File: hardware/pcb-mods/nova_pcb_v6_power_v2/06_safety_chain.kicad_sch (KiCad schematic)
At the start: 23 parts, among them Q2 BSS138_cutoff, Q3 BSS138_estop, Q4 BSS138_jetcut, SW2 Estop_NC_latching, U10 INA226, U11 INA226, U8 LM393, U9 INA226

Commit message: pcb(v6-power-v2): backfill MPN + Manufacturer fields — 100% BOM coverage
All 50 BOM components now carry MPNs from the verified order list:
Yageo RC0603 resistor set (R14 470k = Vishay CRCW0603 DigiKey sub),
Nichicon UPW1E bulk caps, Bourns SRR1260-220M, Infineon IRLB3034PBF,
onsemi BSS138 x3, TI LM393DR, Pololu buck modules (off-board),
GODIY INA226 20A R002 modules with I2C addresses in Manufacturer field,
AMASS XT60H/XT30U, JST B3B-XH-A, Adam Tech BHR-12-VUA, Sullins headers.
ERC: 0 errors (1 expected V7V5_ARM warning). kicad-happy bom_lock: pass.

Co-Authored-By: Claude Fable 5 <noreply@anthropic.com>
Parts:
- C7: MPN (none) -> CC0603KRX7R9BB104; Manufacturer (none) -> Yageo
- Q2, Q3, Q4: MPN (none) -> BSS138; Manufacturer (none) -> onsemi
- R11, R12: MPN (none) -> RC0603FR-074K7L; Manufacturer (none) -> Yageo
- R13, R5, R7, R8, R9: MPN (none) -> RC0603FR-0710KL; Manufacturer (none) -> Yageo
- R14: MPN (none) -> CRCW0603470KFKEA; Manufacturer (none) -> Vishay Dale
- R15: MPN (none) -> RC0603FR-071ML; Manufacturer (none) -> Yageo
- R16, R2: MPN (none) -> RC0603FR-07100KL; Manufacturer (none) -> Yageo
- R3: MPN (none) -> RC0603FR-0722KL; Manufacturer (none) -> Yageo
- R4: MPN (none) -> RC0603FR-0711K3L; Manufacturer (none) -> Yageo
- R6: MPN (none) -> RC0603FR-0712K1L; Manufacturer (none) -> Yageo
- SW2: MPN (none) -> KF301-5.0-2P; Manufacturer (none) -> Generic (Tugermoola kit; wires to Mxuteuk HB2-ES544)
- U10: MPN (none) -> INA226-20A-R002-MODULE; Manufacturer (none) -> GODIYMODULES (Amazon, off-board, addr 0x41)
- U11: MPN (none) -> INA226-20A-R002-MODULE; Manufacturer (none) -> GODIYMODULES (Amazon, off-board, addr 0x44)
- U8: MPN (none) -> LM393DR; Manufacturer (none) -> Texas Instruments
- U9: MPN (none) -> INA226-20A-R002-MODULE; Manufacturer (none) -> GODIYMODULES (Amazon, off-board, addr 0x40)

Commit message: pcb(v6-power-v2): correct C1-C5 to FymuSing (as purchased) + DigiKey PNs from order CSV
Verified against Complete_Digikey_Order_NOVA.csv (16 lines, all match):
R14 470k confirmed Vishay CRCW0603470KFKEA (541-470KHCT-ND).
C1-C5 corrected Nichicon->FymuSing 1000uF/25V (Amazon purchase, 10x17mm).
Remaining 23 parts without DigiKey PN are Amazon/Pololu/AMASS sourced.

Co-Authored-By: Claude Fable 5 <noreply@anthropic.com>
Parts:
- C7: DigiKey (none) -> 311-1344-1-ND
- Q2, Q3, Q4: DigiKey (none) -> BSS138CT-ND
- R11, R12: DigiKey (none) -> 311-4.70KHRCT-ND
- R13, R5, R7, R8, R9: DigiKey (none) -> 311-10.0KHRCT-ND
- R14: DigiKey (none) -> 541-470KHCT-ND
- R15: DigiKey (none) -> 311-1.00MHRCT-ND
- R16, R2: DigiKey (none) -> 311-100KHRCT-ND
- R3: DigiKey (none) -> 311-22.0KHRCT-ND
- R4: DigiKey (none) -> 311-11.3KHRCT-ND
- R6: DigiKey (none) -> 311-12.1KHRCT-ND
- U8: DigiKey (none) -> 296-1015-1-ND
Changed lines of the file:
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@@
 			)
 		)
+		(property "DigiKey" "311-10.0KHRCT-ND" (at 0 0 0)
+			(effects
+				(font
+					(size 1.27 1.27)
+				)
+				(hide yes)
+			)
+		)
 		(pin "1"
 		)
@@
 			)
 		)
+		(property "DigiKey" "311-4.70KHRCT-ND" (at 0 0 0)
+			(effects
+				(font
+					(size 1.27 1.27)
+				)
+				(hide yes)
+			)
+		)
 		(pin "1"
 		)
@@
 			)
 		)
+		(property "DigiKey" "BSS138CT-ND" (at 0 0 0)
+			(effects
+				(font
+					(size 1.27 1.27)
+				)
+				(hide yes)
+			)
+		)
 		(pin "1"
 		)
@@
 			)
 		)
+		(property "DigiKey" "311-10.0KHRCT-ND" (at 0 0 0)
+			(effects
+				(font
+					(size 1.27 1.27)
+				)
+				(hide yes)
+			)
+		)
 		(pin "1"
 		)
@@
 			)
 		)
+		(property "DigiKey" "311-10.0KHRCT-ND" (at 0 0 0)
+			(effects
+				(font
+					(size 1.27 1.27)
+				)
+				(hide yes)
+			)
+		)
 		(pin "1"
 		)
@@
 			)
 		)
+		(property "DigiKey" "296-1015-1-ND" (at 0 0 0)
+			(effects
+				(font
+					(size 1.27 1.27)
+				)
+				(hide yes)
+			)
+		)
 		(pin "8"
 		)
@@
 			)
 		)
+		(property "DigiKey" "311-22.0KHRCT-ND" (at 0 0 0)
+			(effects
+				(font
+					(size 1.27 1.27)
+				)
+				(hide yes)
+			)
+		)
 		(pin "1"
 		)
@@
 			)
 		)
+		(property "DigiKey" "296-1015-1-ND" (at 0 0 0)
+			(effects
+				(font
+					(size 1.27 1.27)
+				)
+				(hide yes)
+			)
+		)
 		(pin "3"
 		)
@@
 			)
 		)
+		(property "DigiKey" "311-4.70KHRCT-ND" (at 0 0 0)
+			(effects
+				(font
+					(size 1.27 1.27)
+				)
+				(hide yes)
+			)
+		)
 		(pin "1"
 		)
@@
 			)
 		)
+		(property "DigiKey" "311-12.1KHRCT-ND" (at 0 0 0)
+			(effects
+				(font
+					(size 1.27 1.27)
+				)
+				(hide yes)
+			)
+		)
 		(pin "1"
 		)
@@
 			)
 		)
+		(property "DigiKey" "311-11.3KHRCT-ND" (at 0 0 0)
+			(effects
+				(font
+					(size 1.27 1.27)
+				)
+				(hide yes)
+			)
+		)
 		(pin "1"
 		)
@@
 			)
 		)
+		(property "DigiKey" "311-10.0KHRCT-ND" (at 0 0 0)
+			(effects
+				(font
+					(size 1.27 1.27)
+				)
+				(hide yes)
+			)
+		)
 		(pin "1"
 		)
@@
 			)
 		)
+		(property "DigiKey" "296-1015-1-ND" (at 0 0 0)
+			(effects
+				(font
+					(size 1.27 1.27)
+				)
+				(hide yes)
+			)
+		)
 		(pin "5"
 		)
@@
 			)
 		)
+		(property "DigiKey" "311-100KHRCT-ND" (at 0 0 0)
+			(effects
+				(font
+					(size 1.27 1.27)
+				)
+				(hide yes)
+			)
+		)
 		(pin "1"
 		)
@@
 			)
 		)
+		(property "DigiKey" "311-10.0KHRCT-ND" (at 0 0 0)
+			(effects
+				(font
+					(size 1.27 1.27)
+				)
+				(hide yes)
+			)
+		)
 		(pin "1"
 		)
@@
 			)
 		)
+		(property "DigiKey" "541-470KHCT-ND" (at 0 0 0)
+			(effects
+				(font
+					(size 1.27 1.27)
+				)
+				(hide yes)
+			)
+		)
 		(pin "1"
 		)
@@
 			)
 		)
+		(property "DigiKey" "311-1.00MHRCT-ND" (at 0 0 0)
+			(effects
+				(font
+					(size 1.27 1.27)
+				)
+				(hide yes)
+			)
+		)
 		(pin "1"
 		)
@@
 			)
 		)
+		(property "DigiKey" "311-1344-1-ND" (at 0 0 0)
+			(effects
+				(font
+					(size 1.27 1.27)
+				)
+				(hide yes)
+			)
+		)
 		(pin "1"
 		)
@@
 			)
 		)
+		(property "DigiKey" "BSS138CT-ND" (at 0 0 0)
+			(effects
+				(font
+					(size 1.27 1.27)
+				)
+				(hide yes)
+			)
+		)
 		(pin "1"
 		)
@@
 			)
 		)
+		(property "DigiKey" "BSS138CT-ND" (at 0 0 0)
+			(effects
+				(font
+					(size 1.27 1.27)
+				)
+				(hide yes)
+			)
+		)
 		(pin "1"
 		)
@@
 			(effects
 				(font
+					(size 1.27 1.27)
+				)
+				(hide yes)
+			)
+		)
+		(property "DigiKey" "311-100KHRCT-ND" (at 0 0 0)
+			(effects
+				(font

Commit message: pcb(v6-power-v2): AssemblyOrder fields + assembly-sequenced iBOM
15-step hand-solder sequence (flat->tall, SMD bottom cluster -> THT top):
0603s -> SOT-23 -> SOIC -> L1 -> INA headers -> headers/JST/IDC ->
screw blocks -> XT30 -> XT60 -> Q1 (Step 10a test first) -> 470uF -> 1000uF.
bom/ibom_assembly.html groups by AssemblyOrder via netlist extra-data.

Co-Authored-By: Claude Fable 5 <noreply@anthropic.com>
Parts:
- C7: AssemblyOrder (none) -> 02 SMD 0603 C
- Q2, Q3, Q4: AssemblyOrder (none) -> 03 SMD SOT-23
- R11, R12, R13, R14, R15, R16, R2, R3, R4, R5, R6, R7, R8, R9: AssemblyOrder (none) -> 01 SMD 0603 R
- SW2: AssemblyOrder (none) -> 10 THT screw block
- U10, U11, U9: AssemblyOrder (none) -> 06 INA header (4-pin)
- U8: AssemblyOrder (none) -> 04 SMD SOIC-8
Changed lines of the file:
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@@
 			)
 		)
+		(property "AssemblyOrder" "01 SMD 0603 R" (at 0 0 0)
+			(effects
+				(font
+					(size 1.27 1.27)
+				)
+				(hide yes)
+			)
+		)
 		(pin "1"
 		)
@@
 			)
 		)
+		(property "AssemblyOrder" "01 SMD 0603 R" (at 0 0 0)
+			(effects
+				(font
+					(size 1.27 1.27)
+				)
+				(hide yes)
+			)
+		)
 		(pin "1"
 		)
@@
 			)
 		)
+		(property "AssemblyOrder" "03 SMD SOT-23" (at 0 0 0)
+			(effects
+				(font
+					(size 1.27 1.27)
+				)
+				(hide yes)
+			)
+		)
 		(pin "1"
 		)
@@
 			)
 		)
+		(property "AssemblyOrder" "06 INA header (4-pin)" (at 0 0 0)
+			(effects
+				(font
+					(size 1.27 1.27)
+				)
+				(hide yes)
+			)
+		)
 		(pin "1"
 		)
@@
 			)
 		)
+		(property "AssemblyOrder" "01 SMD 0603 R" (at 0 0 0)
+			(effects
+				(font
+					(size 1.27 1.27)
+				)
+				(hide yes)
+			)
+		)
 		(pin "1"
 		)
@@
 			)
 		)
+		(property "AssemblyOrder" "01 SMD 0603 R" (at 0 0 0)
+			(effects
+				(font
+					(size 1.27 1.27)
+				)
+				(hide yes)
+			)
+		)
 		(pin "1"
 		)
@@
 			)
 		)
+		(property "AssemblyOrder" "04 SMD SOIC-8" (at 0 0 0)
+			(effects
+				(font
+					(size 1.27 1.27)
+				)
+				(hide yes)
+			)
+		)
 		(pin "8"
 		)
@@
 			)
 		)
+		(property "AssemblyOrder" "01 SMD 0603 R" (at 0 0 0)
+			(effects
+				(font
+					(size 1.27 1.27)
+				)
+				(hide yes)
+			)
+		)
 		(pin "1"
 		)
@@
 			)
 		)
+		(property "AssemblyOrder" "04 SMD SOIC-8" (at 0 0 0)
+			(effects
+				(font
+					(size 1.27 1.27)
+				)
+				(hide yes)
+			)
+		)
 		(pin "3"
 		)
@@
 			)
 		)
+		(property "AssemblyOrder" "06 INA header (4-pin)" (at 0 0 0)
+			(effects
+				(font
+					(size 1.27 1.27)
+				)
+				(hide yes)
+			)
+		)
 		(pin "1"
 		)
@@
 			)
 		)
+		(property "AssemblyOrder" "01 SMD 0603 R" (at 0 0 0)
+			(effects
+				(font
+					(size 1.27 1.27)
+				)
+				(hide yes)
+			)
+		)
 		(pin "1"
 		)
@@
 			)
 		)
+		(property "AssemblyOrder" "01 SMD 0603 R" (at 0 0 0)
+			(effects
+				(font
+					(size 1.27 1.27)
+				)
+				(hide yes)
+			)
+		)
 		(pin "1"
 		)
@@
 			)
 		)
+		(property "AssemblyOrder" "01 SMD 0603 R" (at 0 0 0)
+			(effects
+				(font
+					(size 1.27 1.27)
+				)
+				(hide yes)
+			)
+		)
 		(pin "1"
 		)
@@
 			)
 		)
+		(property "AssemblyOrder" "01 SMD 0603 R" (at 0 0 0)
+			(effects
+				(font
+					(size 1.27 1.27)
+				)
+				(hide yes)
+			)
+		)
 		(pin "1"
 		)
@@
 			)
 		)
+		(property "AssemblyOrder" "04 SMD SOIC-8" (at 0 0 0)
+			(effects
+				(font
+					(size 1.27 1.27)
+				)
+				(hide yes)
+			)
+		)
 		(pin "5"
 		)
@@
 			)
 		)
+		(property "AssemblyOrder" "01 SMD 0603 R" (at 0 0 0)
+			(effects
+				(font
+					(size 1.27 1.27)
+				)
+				(hide yes)
+			)
+		)
 		(pin "1"
 		)
@@
 			)
 		)
+		(property "AssemblyOrder" "06 INA header (4-pin)" (at 0 0 0)
+			(effects
+				(font
+					(size 1.27 1.27)
+				)
+				(hide yes)
+			)
+		)
 		(pin "1"
 		)
@@
 			)
 		)
+		(property "AssemblyOrder" "10 THT screw block" (at 0 0 0)
+			(effects
+				(font
+					(size 1.27 1.27)
+				)
+				(hide yes)
+			)
+		)
 		(pin "1"
 		)
@@
 			)
 		)
+		(property "AssemblyOrder" "01 SMD 0603 R" (at 0 0 0)
+			(effects
+				(font
+					(size 1.27 1.27)
+				)
+				(hide yes)
+			)
+		)
 		(pin "1"
 		)
@@
 			)
 		)
+		(property "AssemblyOrder" "01 SMD 0603 R" (at 0 0 0)
+			(effects
+				(font
+					(size 1.27 1.27)
+				)
+				(hide yes)
+			)
+		)
 		(pin "1"
 		)
@@
 			)
 		)
+		(property "AssemblyOrder" "01 SMD 0603 R" (at 0 0 0)
+			(effects
+				(font
+					(size 1.27 1.27)
+				)
+				(hide yes)
+			)
+		)
 		(pin "1"
 		)
@@
 			)
 		)
+		(property "AssemblyOrder" "02 SMD 0603 C" (at 0 0 0)
+			(effects
+				(font
+					(size 1.27 1.27)
+				)
+				(hide yes)
+			)
+		)
 		(pin "1"
 		)
@@
 			)
 		)
+		(property "AssemblyOrder" "03 SMD SOT-23" (at 0 0 0)
+			(effects
+				(font
+					(size 1.27 1.27)
+				)
+				(hide yes)
+			)
+		)
 		(pin "1"
 		)
@@
 			)
 		)
+		(property "AssemblyOrder" "03 SMD SOT-23" (at 0 0 0)
+			(effects
+				(font
+					(size 1.27 1.27)
+				)
+				(hide yes)
+			)
+		)
 		(pin "1"
 		)
@@
 			(effects
 				(font
+					(size 1.27 1.27)
+				)
+				(hide yes)
+			)
+		)
+		(property "AssemblyOrder" "01 SMD 0603 R" (at 0 0 0)
+			(effects
+				(font

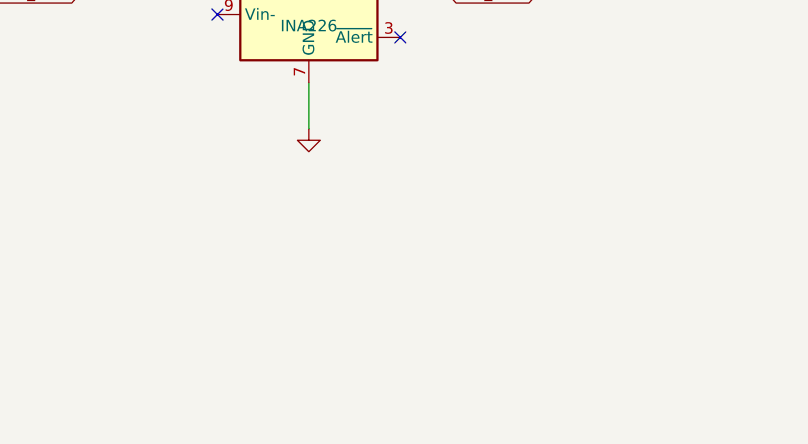
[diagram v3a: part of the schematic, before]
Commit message: power board: arm Phase-4 schematic edits (EN re-gate + J14 + arm INA226) + README status
Commits the ERC-clean (0/0) arm Phase-4 schematic work that had been uncommitted
all session (and nearly lost to a stray stash):
- 02_power_rails: U5.EN re-gated VBAT_PROTECTED->EN_BUCKS (arm buck now under the
  same E-stop/undervoltage chain as legs); J14 arm-output XT30 (fixes the former
  dangling V7V5_ARM single-pad net).
- 06_safety_chain: U12 arm-rail INA226 (addr 0x45, DNP Phase-4) + no-connects.
- README status line refreshed to match reality + point at STATUS.md.

The .kicad_pcb is intentionally NOT included — those footprints are F8'd but
still need GUI placement + routing (tracked as blocker B1 in STATUS.md).

Co-Authored-By: Claude Opus 4.8 <noreply@anthropic.com>
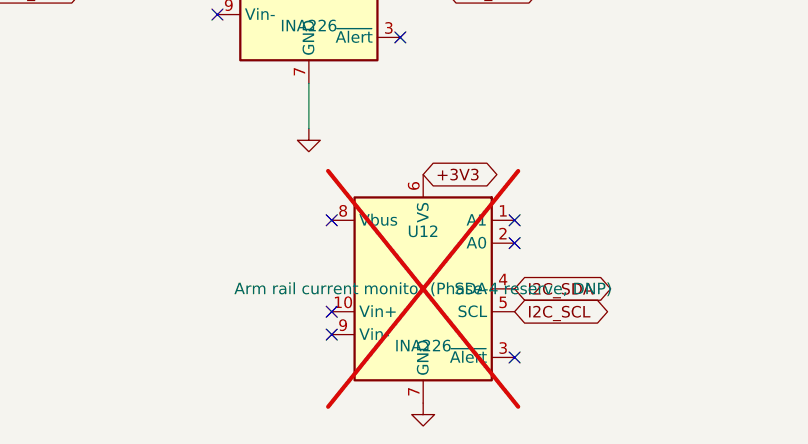
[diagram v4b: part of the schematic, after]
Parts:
- added U12: INA226, nova_v6:INA226_Module_Breakout, symbol Sensor_Energy:INA226
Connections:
- net +3V3: now also U12.6 (VS)
- net GND: now also U12.7 (GND)
- net I2C_SCL: now also U12.5 (SCL)
- net I2C_SDA: now also U12.4 (SDA)
- no-connect marks 18 -> 24
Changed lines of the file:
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@@
 		)
+	)
+	(symbol
+		(lib_id "Sensor_Energy:INA226")
+		(at 165.1 200.66 0)
+		(unit 1)
+		(exclude_from_sim no)
+		(in_bom yes)
+		(on_board yes)
+		(dnp yes)
+		(property "Reference" "U12"
+			(at 165.1 194.31 0)
+			(effects (font (size 1.27 1.27)))
+		)
+		(property "Value" "INA226"
+			(at 165.1 207.01 0)
+			(effects (font (size 1.27 1.27)))
+		)
+		(property "Footprint" "nova_v6:INA226_Module_Breakout"
+			(at 165.1 200.66 0)
+			(effects (font (size 1.27 1.27)) (hide yes))
+		)
+		(property "Datasheet" "~"
+			(at 165.1 200.66 0)
+			(effects (font (size 1.27 1.27)) (hide yes))
+		)
+		(property "Description" "Arm rail current monitor (Phase-4 reserve, DNP)"
+			(at 165.1 200.66 0)
+			(effects (font (size 1.27 1.27)))
+		)
+		(property "Manufacturer" "GODIYMODULES (Amazon, off-board, addr 0x45 - DNP Phase-4 arm)" (at 0 0 0)
+			(effects (font (size 1.27 1.27)) (hide yes))
+		)
+		(property "MPN" "INA226-20A-R002-MODULE" (at 0 0 0)
+			(effects (font (size 1.27 1.27)) (hide yes))
+		)
+		(property "AssemblyOrder" "06 INA header (4-pin) - Phase-4 DNP" (at 0 0 0)
+			(effects (font (size 1.27 1.27)) (hide yes))
+		)
+		(pin "1"
+		)
+		(pin "2"
+		)
+		(pin "3"
+		)
+		(pin "4"
+		)
+		(pin "5"
+		)
+		(pin "6"
+		)
+		(pin "7"
+		)
+		(pin "8"
+		)
+		(pin "9"
+		)
+		(pin "10"
+		)
+		(instances
+			(project "nova_pcb_v6_power_v2"
+				(path "/f535083b-f621-4317-a378-cf746e7f972b/38477265-f64f-4f2e-aefb-289b79c664e1"
+					(reference "U12")
+					(unit 1)
+				)
+			)
+		)
+	)
+	(global_label "I2C_SDA"
+		(shape bidirectional)
+		(at 175.26 200.66 0)
+		(effects
+			(font
+				(size 1.27 1.27)
+			)
+			(justify left)
+		)
+		(property "Intersheetrefs" "${INTERSHEET_REFS}"
+			(at 175.26 200.66 0)
+			(effects
+				(font
+					(size 1.27 1.27)
+				)
+				(hide yes)
+			)
+		)
+	)
+	(global_label "I2C_SCL"
+		(shape bidirectional)
+		(at 175.26 203.2 0)
+		(effects
+			(font
+				(size 1.27 1.27)
+			)
+			(justify left)
+		)
+		(property "Intersheetrefs" "${INTERSHEET_REFS}"
+			(at 175.26 203.2 0)
+			(effects
+				(font
+					(size 1.27 1.27)
+				)
+				(hide yes)
+			)
+		)
+	)
+	(global_label "+3V3"
+		(shape bidirectional)
+		(at 165.1 187.96 0)
+		(effects
+			(font
+				(size 1.27 1.27)
+			)
+			(justify left)
+		)
+		(property "Intersheetrefs" "${INTERSHEET_REFS}"
+			(at 165.1 187.96 0)
+			(effects
+				(font
+					(size 1.27 1.27)
+				)
+				(hide yes)
+			)
+		)
+	)
+	(symbol
+		(lib_id "power:GND")
+		(at 165.1 213.35999999999999 0)
+		(unit 1)
+		(exclude_from_sim no)
+		(in_bom yes)
+		(on_board yes)
+		(dnp no)
+		(property "Reference" "#PWR616"
+			(at 171.45 213.35999999999999 270)
+			(effects (font (size 1.27 1.27)) (hide yes))
+		)
+		(property "Value" "GND"
+			(at 158.75 213.35999999999999 270)
+			(effects (font (size 1.27 1.27)) (hide yes))
+		)
+		(property "Footprint" ""
+			(at 165.1 213.35999999999999 0)
+			(effects (font (size 1.27 1.27)) (hide yes))
+		)
+		(property "Datasheet" "~"
+			(at 165.1 213.35999999999999 0)
+			(effects (font (size 1.27 1.27)) (hide yes))
+		)
+		(property "Description" ""
+			(at 165.1 213.35999999999999 0)
+			(effects (font (size 1.27 1.27)))
+		)
+		(pin "1"
+		)
+		(instances
+			(project "nova_pcb_v6_power_v2"
+				(path "/f535083b-f621-4317-a378-cf746e7f972b/38477265-f64f-4f2e-aefb-289b79c664e1"
+					(reference "#PWR616")
+					(unit 1)
+				)
+			)
+		)
+	)
+	(no_connect
+		(at 154.94 193.04)
+	)
+	(no_connect
+		(at 154.94 203.2)
+	)
+	(no_connect
+		(at 154.94 205.74)
+	)
+	(no_connect
+		(at 175.26 193.04)
+	)
+	(no_connect
+		(at 175.26 195.58)
+	)
+	(no_connect
+		(at 175.26 208.28)
 	)
 	(sheet_instances

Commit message: Chassis + leg_v6 CAD: no-drill assembly, leg fault audit (LA-1..28 + #47), fastener + gate hardening (#48)
* power board: arm Phase-4 routed + cleaned + fresh gerbers (fab-ready)

Completes the power board (blocker B1):
- U5.EN routed on EN_BUCKS (re-gate now realized on the board).
- V7V5_ARM 3mm, BATT_NEG/VBAT long runs 3mm, 21 high-current pads solid
  zone-connection (current-capacity fixes; TO-220/SW1 escapes left at 1.3mm).
- Removed the duplicate U12 + J14 (F8 UUID-mismatch artifacts) and the full
  orphan dangling-track chain they left behind.
- DRC: 0 hard, 0 unconnected, 0 dangling (10 cosmetic silk/lib only).
- Gerbers regenerated; fab_gate GO on both boards (J20 cross-board match OK).

DNP roster correct (U5 arm buck, U12 arm INA = Phase-4 reserve).

Co-Authored-By: Claude Opus 4.8 <noreply@anthropic.com>

* audit fixes 2026-06-18: NaN guard, pinout/battery/LVC doc sync, STATUS audit block

- main.cpp: NaN guard on commanded position (was UB (uint16_t)NaN -> 0 slam)
- teensy firmware/README.md: pinout table corrected to match main.cpp/PCB v6 (Serial1 0/1, E-stop 5, batt 4, active-LOW OE)
- power-budget.md + BOM.md: battery 4000->6000mAh (real Ovonic packs) + runtime/charge recompute
- BOM.md: bus driver order line -> SN74LVC125A (must be LVC, not 74HC125)
- STATUS.md: cross-domain audit section (open misalignments, weak points, questions)

Co-Authored-By: Claude Opus 4.8 <noreply@anthropic.com>

* docs: add servo-bus half-duplex timing bench checklist (pre-power-on §10)

Co-Authored-By: Claude Opus 4.8 <noreply@anthropic.com>

* docs: battery 4000->6000mAh sweep across secondary docs + STATUS CI-note fix

- 6000mAh 4S Ovonic (real pack) in cad-tooling, notes-qol (SoC math 5400mAh),
  order-list (bag), wiring diagram, README charger note, patterns pocket label
- dimensions.md + patterns.md: physical box/pocket dims flagged RE-MEASURE
  (6000mAh pack is larger; old 4000mAh dims kept as reference, not as truth)
- STATUS.md: corrected CI note (ros-pytest.yml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
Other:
- moved on the sheet: R11, R13, U12

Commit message: pcb: clear U12's stale DNP flag — v1 populates it as the L2 monitor at 0x45 (#242) (#361)
U12 was flagged do-not-populate in BOTH the schematic and the board. The
4th INA226 stopped being an arm part on 2026-06-30 when it was reassigned
to the L2 LiDAR rail: -D NOVA_INA226_L2 is set, ina226_telemetry.h
declares INA226_ADDR_L2 = 0x45, /power_rails was widened 9 -> 12 floats
for it, and BUILD_PLAN §4 says to fit it at stage 10. The flag never
followed.

TWO SITES, both edited as TEXT:
  06_safety_chain.kicad_sch   (dnp yes) -> (dnp no)          [U12 symbol]
  nova_pcb_v6_power_v2.kicad_pcb  (attr through_hole dnp) -> (attr through_hole)

The board stores DNP as a flag inside (attr ...), NOT as a (dnp) token --
a text grep for "(dnp" finds nothing on the board while pcbnew's IsDNP()
reports it. Worth writing down: grepping the board text is the wrong
instrument for this attribute.

Text-edited rather than cleared in the schematic and pushed with Update
PCB from Schematic, because footprint round-trips on this board are
recorded as silently reverting SW1's drill 1.5 -> 1.2mm (board-vs-gerber
mismatch, caught only in pre-fab review last time). SW1 re-verified at
1.500 x 1.500 after the edit, as that rule requires.

U12 already had (in_bom yes) and (on_board yes), so the single token was
the whole fix.

VERIFIED, each against a pre-edit baseline:
  pcbnew IsDNP()      ['U12','U5'] -> ['U5']
  fab_gate.py         DNP roster assertion now PASSES; whole gate GO
  BOM default         U12's DNP column "DNP" -> "" (still 62 rows)
  BOM --exclude-dnp   60 -> 61 rows, U12 now PRESENT
  ERC                 exit 0, 0 violations
  SW1 drill           1.500 x 1.500, unchanged

fab_gate's EXPECTED_DNP already listed only U5 for this board, with a
comment naming this exact stale flag as the thing the assertion exists to
surface. It was doing its job; nobody had run it since. The gate was red
on this and is now green.

⚠️ This commit also carries pre-existing KiCad-9 normalisation of th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
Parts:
- U12: now fitted
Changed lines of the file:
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@@
 		(in_bom yes)
 		(on_board yes)
-		(dnp yes)
+		(dnp no)
 		(property "Reference" "U12"
 			(at 224.79 91.44 0)
